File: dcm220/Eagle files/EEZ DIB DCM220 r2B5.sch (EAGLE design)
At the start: 245 parts, among them IC1 Si8662AB-B-IS1, IC10 MC33272ADR2G, IC11 LT3763EFE#PBF, IC12 MC33274ADR2G, IC13 LT3763EFE#PBF, IC2 TPS54060DGQ, IC3 Si8641AB-B-IS1, IC4 M24C32-WMN6P, IC5 LP2985-33DBVR, IC6 74HC2G04GW,125, IC7 N.C., IC8 STM32F373C8T6, IC9 TL431B, J1 4907, J2 571-0500, J3 571-0100, J4 571-0500, J5 571-0100, Q1 BSP716NH6327XTSA1, Q10 BSS84, Q2 NTD5867NLT4G, Q3 NTD5867NLT4G, Q4 BSS205NH6327XTSA1, Q5 BSS84, Q6 BSP716NH6327XTSA1, Q7 NTD5867NLT4G, Q8 NTD5867NLT4G, Q9 BSS205NH6327XTSA1, X1 39-30-1020, X2 77317-104-28LF, X3 N.C., X4 DS1024-2*5R0, Y1 LF XTAL026392

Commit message: DCM220 r2B5
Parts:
- removed SH1, SH3, SH4: (no value), EEZ_Lib1:SHORTNOHOLE
- R30, R32, R54, R56: value 22K -> 20K
- R31, R33, R55, R57: value 10K -> 12K
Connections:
- removed net DC_OUT-: C2.1, C46.-, C50.2, C52.2, C57.2, C59.2, C60.2, C61.-, C62.-, C63.2, C68.-, C71.2, C72.2, C77.2, C79.2, C80.2, C81.-, C82.-, C83.2, CH1.GND, CH2.GND, D12.A, D7.A, J3.1, J5.1, L1-2.2, LED1.C, LED2.C, Q3.S, Q8.S, R37.1, R41.2, R61.1, R65.2, SH1.GND_B, SH3.GND_A, SH4.GND_A, X4-1.1, X4-10.1, X4-2.1, X4-3.1, X4-4.1, X4-5.1, X4-6.1, X4-7.1, X4-8.1, X4-9.1, ZD1.A, ZD3.A, ZD5.A
- net +VREF: now also IC8.VDDA/VREF+
- net AGND: now also IC9.A
- net GND: now also C2.1, C46.-, C50.2, C52.2, C57.2, C59.2, C60.2, C61.-, C62.-, C63.2, C68.-, C71.2, C72.2, C77.2, C79.2, C80.2, C81.-, C82.-, C83.2, CH1.GND, CH2.GND, D12.A, D7.A, J3.1, J5.1, L1-2.2, LED1.C, LED2.C, Q3.S, Q8.S, R37.1, R41.2, R61.1, R65.2, X4-1.1, X4-10.1, X4-2.1, X4-3.1, X4-4.1, X4-5.1, X4-6.1, X4-7.1, X4-8.1, X4-9.1, ZD1.A, ZD3.A, ZD5.A; no longer IC9.A, SH1.GND_A, SH3.GND_B, SH4.GND_B
- net VDDA: no longer IC8.VDDA/VREF+
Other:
- moved on the sheet: FB1

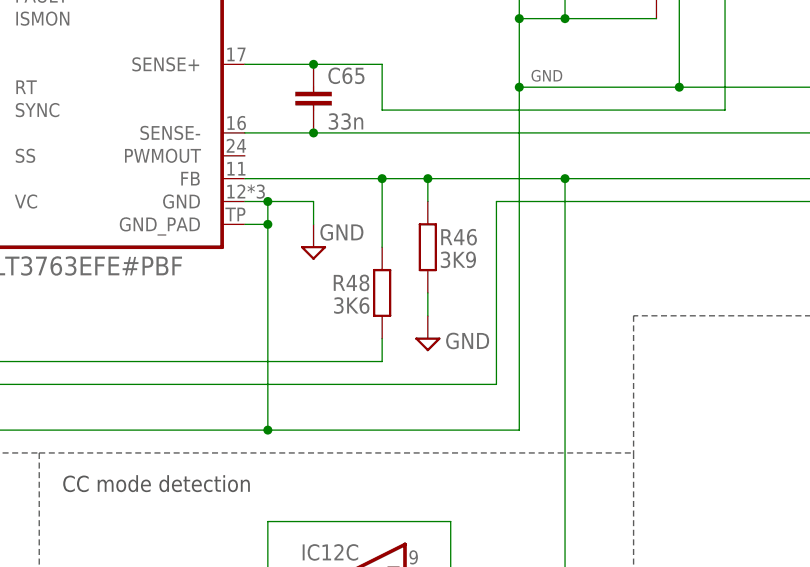
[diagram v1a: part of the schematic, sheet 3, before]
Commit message: DCM220 modified U_SET dividers
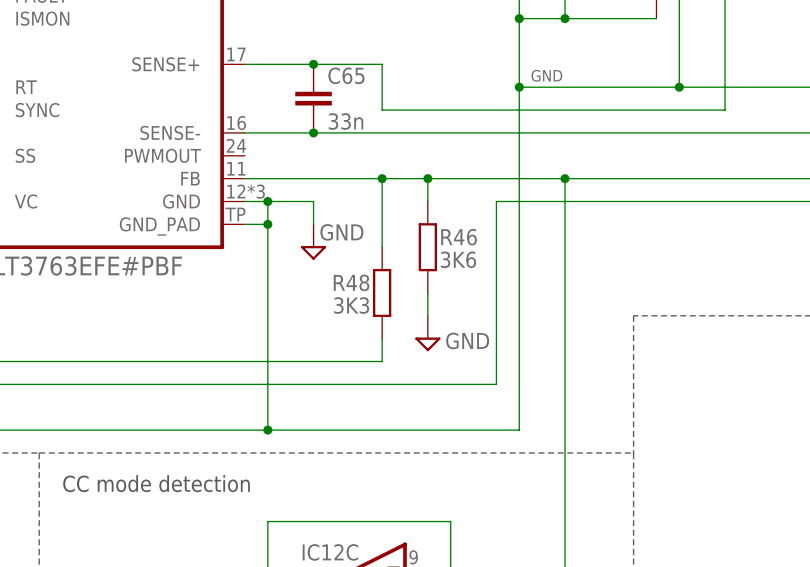
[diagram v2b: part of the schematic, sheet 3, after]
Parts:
- R46, R70: value 3K9 -> 3K6
- R48, R72: value 3K6 -> 3K3
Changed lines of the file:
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@@
 <part name="C54" library="rcl" deviceset="C-EU" device="C0805" value="220n"/>
 <part name="R39" library="rcl" deviceset="R-EU_" device="R0805" value="30K"/>
-<part name="R46" library="rcl" deviceset="R-EU_" device="R0805" value="3K9"/>
+<part name="R46" library="rcl" deviceset="R-EU_" device="R0805" value="3K6"/>
 <part name="SUPPLY15" library="supply2" deviceset="GND" device=""/>
-<part name="R48" library="rcl" deviceset="R-EU_" device="R0805" value="3K6"/>
+<part name="R48" library="rcl" deviceset="R-EU_" device="R0805" value="3K3"/>
 <part name="C46" library="EEZ_Lib1" deviceset="ECAP" device="SMD8.3MM/HA0" value="EEEFK1H470"/>
 <part name="C52" library="rcl" deviceset="C-EU" device="C1210" value="10u"/>
@@
 <part name="C74" library="rcl" deviceset="C-EU" device="C0805" value="220n"/>
 <part name="R63" library="rcl" deviceset="R-EU_" device="R0805" value="30K"/>
-<part name="R70" library="rcl" deviceset="R-EU_" device="R0805" value="3K9"/>
+<part name="R70" library="rcl" deviceset="R-EU_" device="R0805" value="3K6"/>
 <part name="SUPPLY25" library="supply2" deviceset="GND" device=""/>
-<part name="R72" library="rcl" deviceset="R-EU_" device="R0805" value="3K6"/>
+<part name="R72" library="rcl" deviceset="R-EU_" device="R0805" value="3K3"/>
 <part name="C68" library="EEZ_Lib1" deviceset="ECAP" device="SMD8.3MM/HA0" value="EEEFK1H470"/>
 <part name="C72" library="rcl" deviceset="C-EU" device="C1210" value="10u"/>
